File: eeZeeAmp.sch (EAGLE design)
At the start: 15 parts, among them IC1 LM386

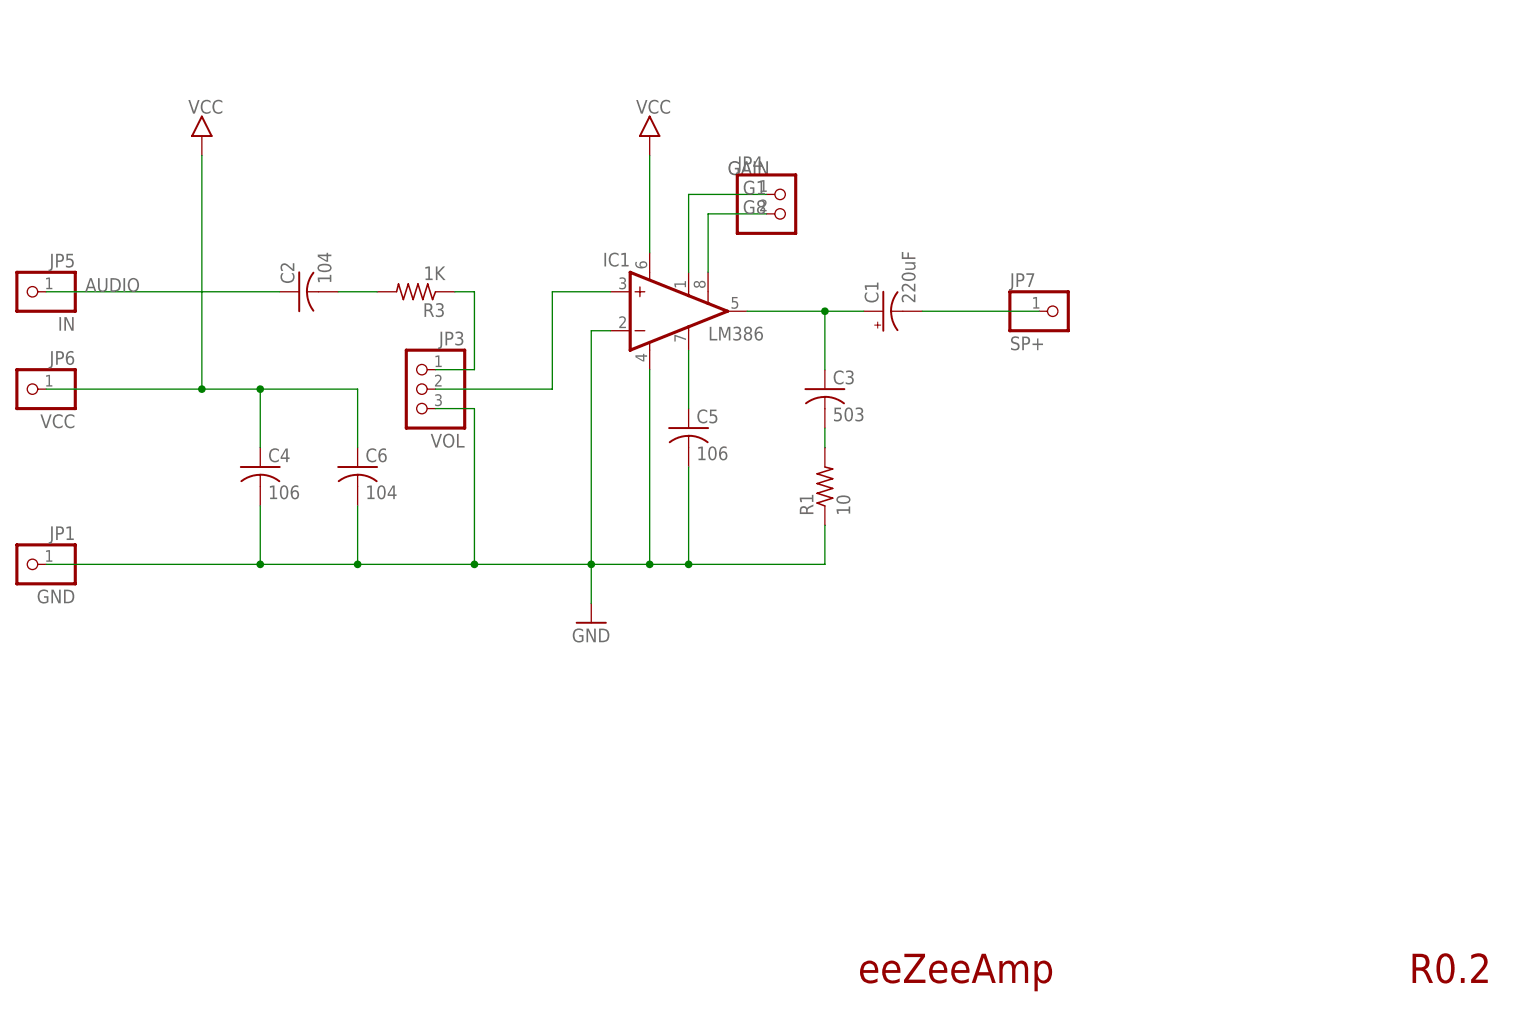
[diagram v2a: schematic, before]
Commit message: Separated gain pin header into individual pins
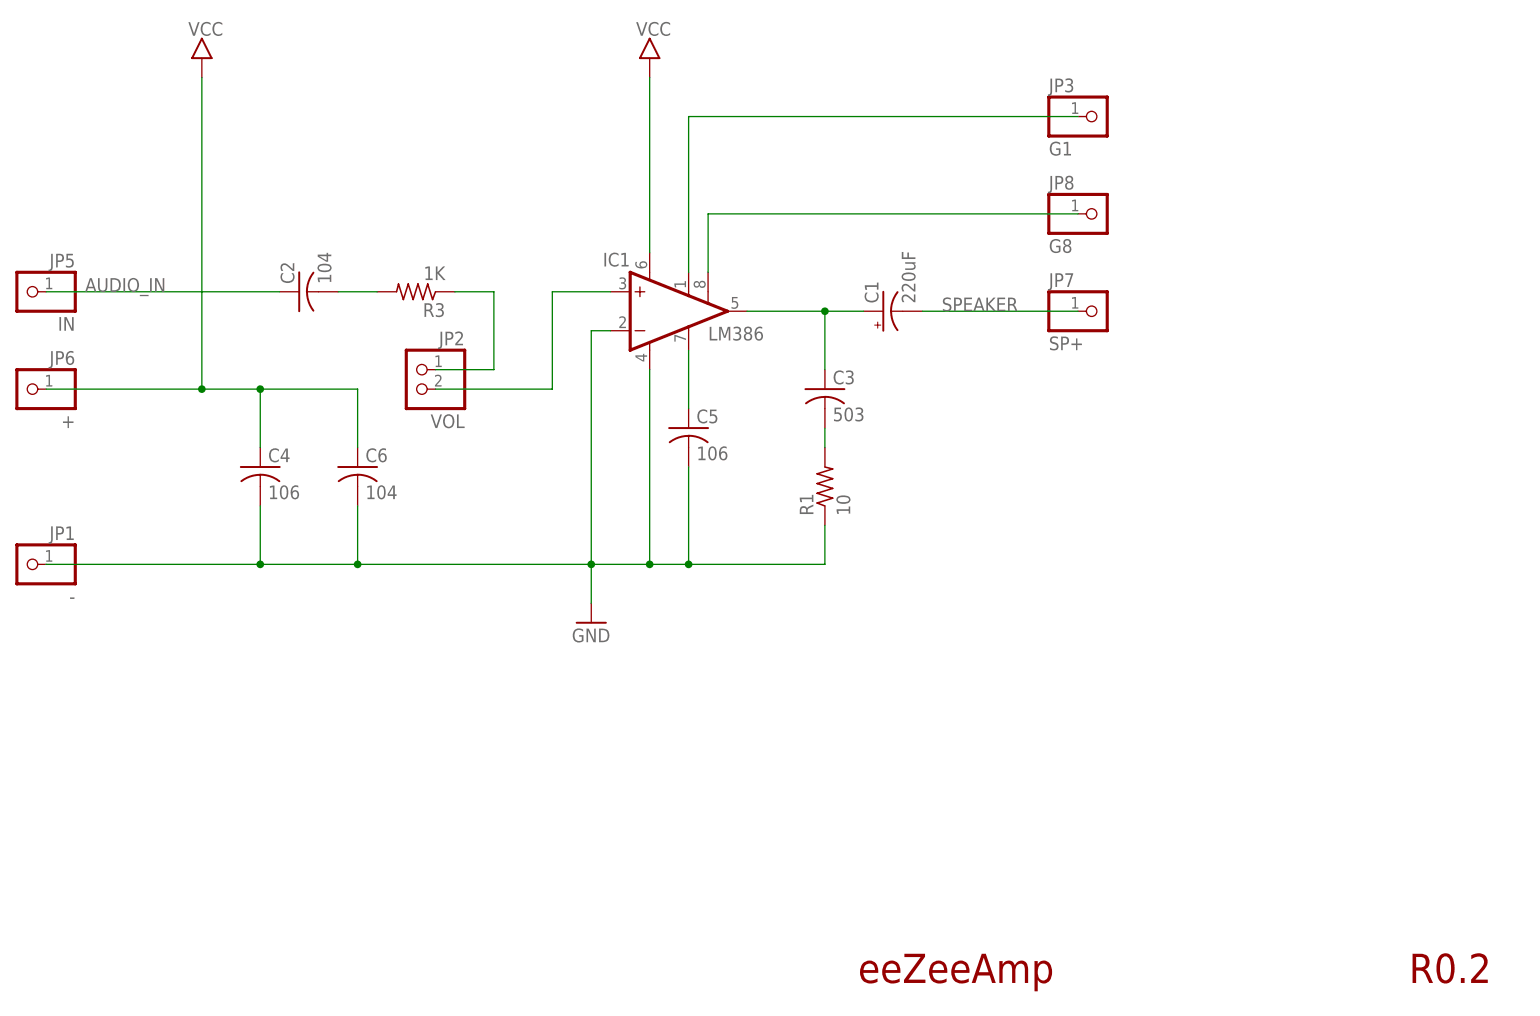
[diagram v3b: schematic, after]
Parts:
- removed JP4: (no value), pinhead-2:PINHD-1X02_2.54-S
- added JP2: VOL, pinhead-2:PINHD-1X02_2.54-S
- added JP8: G8, pinhead-2:PINHD-1X01_2.54-S
- JP1: value GND -> -
- JP3: value VOL -> G1; device pinhead-2:PINHD-1X03_2.54-S -> pinhead-2:PINHD-1X01_2.54-S
- JP6: value VCC -> +
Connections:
- net AUDIO renamed AUDIO_IN
- net SP+ renamed SPEAKER
- net G1: now also JP3.1; no longer JP4.1
- net G8: now also JP8.1; no longer JP4.2
- net GND: no longer JP3.3
- net N$1: now also JP2.2; no longer JP3.2
- net N$8: now also JP2.1; no longer JP3.1
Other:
- note removed: "GAIN"
- moved on the sheet: JP7
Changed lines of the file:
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@@
 <part name="FRAME1" library="bt" deviceset="LETTER_L" device=""/>
 <part name="C6" library="rcl" deviceset="C-US" device="C0603" value="104"/>
-<part name="JP3" library="pinhead-2" deviceset="PINHD-1X03" device="_2.54-S" value="VOL"/>
-<part name="JP4" library="pinhead-2" deviceset="PINHD-1X02" device="_2.54-S"/>
 <part name="JP5" library="pinhead-2" deviceset="PINHD-1X01" device="_2.54-S" value="IN"/>
-<part name="JP6" library="pinhead-2" deviceset="PINHD-1X01" device="_2.54-S" value="VCC"/>
+<part name="JP6" library="pinhead-2" deviceset="PINHD-1X01" device="_2.54-S" value="+"/>
 <part name="JP7" library="pinhead-2" deviceset="PINHD-1X01" device="_2.54-S" value="SP+"/>
-<part name="JP1" library="pinhead-2" deviceset="PINHD-1X01" device="_2.54-S" value="GND"/>
+<part name="JP1" library="pinhead-2" deviceset="PINHD-1X01" device="_2.54-S" value="-"/>
+<part name="JP2" library="pinhead-2" deviceset="PINHD-1X02" device="_2.54-S" value="VOL"/>
+<part name="JP3" library="pinhead-2" deviceset="PINHD-1X01" device="_2.54-S" value="G1"/>
+<part name="JP8" library="pinhead-2" deviceset="PINHD-1X01" device="_2.54-S" value="G8"/>
 </parts>
 <sheets>
@@
 <text x="159.258" y="24.13" size="3.81" layer="94">eeZeeAmp</text>
 <text x="231.14" y="24.13" size="3.81" layer="94">R0.2</text>
-<text x="142.24" y="129.54" size="1.778" layer="97">GAIN</text>
 </plain>
 <instances>
@@
 <instance part="R1" gate="G$1" x="154.94" y="88.9" rot="R90"/>
 <instance part="R3" gate="G$1" x="101.6" y="114.3" rot="R180"/>
-<instance part="U$1" gate="G$1" x="132.08" y="132.08"/>
-<instance part="U$2" gate="G$1" x="73.66" y="132.08"/>
+<instance part="U$1" gate="G$1" x="132.08" y="142.24"/>
+<instance part="U$2" gate="G$1" x="73.66" y="142.24"/>
 <instance part="C4" gate="G$1" x="81.28" y="91.44"/>
 <instance part="GND1" gate="1" x="124.46" y="71.12"/>
@@
 <instance part="FRAME1" gate="G$2" x="147.32" y="2.54"/>
 <instance part="C6" gate="G$1" x="93.98" y="91.44"/>
-<instance part="JP3" gate="A" x="101.6" y="101.6" rot="MR0"/>
-<instance part="JP4" gate="A" x="149.86" y="124.46"/>
 <instance part="JP5" gate="A" x="50.8" y="114.3" rot="MR0"/>
 <instance part="JP6" gate="A" x="50.8" y="101.6" rot="MR0"/>
-<instance part="JP7" gate="A" x="185.42" y="111.76"/>
+<instance part="JP7" gate="A" x="190.5" y="111.76"/>
 <instance part="JP1" gate="A" x="50.8" y="78.74" rot="MR0"/>
+<instance part="JP2" gate="A" x="101.6" y="101.6" rot="MR0"/>
+<instance part="JP3" gate="A" x="190.5" y="137.16"/>
+<instance part="JP8" gate="A" x="190.5" y="124.46"/>
 </instances>
 <busses>
@@
 <wire x1="127" y1="114.3" x2="119.38" y2="114.3" width="0.1524" layer="91"/>
 <wire x1="119.38" y1="114.3" x2="119.38" y2="101.6" width="0.1524" layer="91"/>
-<pinref part="JP3" gate="A" pin="2"/>
 <wire x1="119.38" y1="101.6" x2="104.14" y2="101.6" width="0.1524" layer="91"/>
+<pinref part="JP2" gate="A" pin="2"/>
 </segment>
 </net>
@@
 </segment>
 </net>
-<net name="SP+" class="0">
+<net name="SPEAKER" class="0">
 <segment>
 <pinref part="C1" gate="G$1" pin="-"/>
-<wire x1="167.64" y1="111.76" x2="182.88" y2="111.76" width="0.1524" layer="91"/>
+<wire x1="167.64" y1="111.76" x2="187.96" y2="111.76" width="0.1524" layer="91"/>
 <pinref part="JP7" gate="A" pin="1"/>
+<label x="170.18" y="111.76" size="1.778" layer="95"/>
 </segment>
 </net>
@@
 <segment>
 <pinref part="R3" gate="G$1" pin="1"/>
-<wire x1="106.68" y1="114.3" x2="109.22" y2="114.3" width="0.1524" layer="91"/>
-<pinref part="JP3" gate="A" pin="1"/>
-<wire x1="104.14" y1="104.14" x2="109.22" y2="104.14" width="0.1524" layer="91"/>
-<wire x1="109.22" y1="104.14" x2="109.22" y2="114.3" width="0.1524" layer="91"/>
+<wire x1="106.68" y1="114.3" x2="111.76" y2="114.3" width="0.1524" layer="91"/>
+<wire x1="104.14" y1="104.14" x2="111.76" y2="104.14" width="0.1524" layer="91"/>
+<wire x1="111.76" y1="104.14" x2="111.76" y2="114.3" width="0.1524" layer="91"/>
+<pinref part="JP2" gate="A" pin="1"/>
 </segment>
 </net>
@@
 <segment>
 <pinref part="IC1" gate="G$1" pin="VS"/>
-<wire x1="132.08" y1="119.38" x2="132.08" y2="132.08" width="0.1524" layer="91"/>
+<wire x1="132.08" y1="119.38" x2="132.08" y2="142.24" width="0.1524" layer="91"/>
 <pinref part="U$1" gate="G$1" pin="VCC"/>
 </segment>
 <segment>
-<wire x1="73.66" y1="101.6" x2="73.66" y2="132.08" width="0.1524" layer="91"/>
+<wire x1="73.66" y1="101.6" x2="73.66" y2="142.24" width="0.1524" layer="91"/>
 <pinref part="U$2" gate="G$1" pin="VCC"/>
 <wire x1="53.34" y1="101.6" x2="73.66" y2="101.6" width="0.1524" layer="91"/>
@@
 </segment>
 </net>
-<net name="AUDIO" class="0">
+<net name="AUDIO_IN" class="0">
 <segment>
 <pinref part="C2" gate="G$1" pin="1"/>
@@
 <net name="GND" class="0">
 <segment>
-<wire x1="109.22" y1="99.06" x2="109.22" y2="78.74" width="0.1524" layer="91"/>
 <pinref part="R1" gate="G$1" pin="1"/>
-<wire x1="109.22" y1="78.74" x2="124.46" y2="78.74" width="0.1524" layer="91"/>
 <wire x1="124.46" y1="78.74" x2="132.08" y2="78.74" width="0.1524" layer="91"/>
 <wire x1="132.08" y1="78.74" x2="137.16" y2="78.74" width="0.1524" layer="91"/>
@@
 <junction x="124.46" y="78.74"/>
 <wire x1="53.34" y1="78.74" x2="81.28" y2="78.74" width="0.1524" layer="91"/>
-<junction x="109.22" y="78.74"/>
 <pinref part="C4" gate="G$1" pin="2"/>
 <wire x1="81.28" y1="78.74" x2="93.98" y2="78.74" width="0.1524" layer="91"/>
-<wire x1="93.98" y1="78.74" x2="109.22" y2="78.74" width="0.1524" layer="91"/>
+<wire x1="93.98" y1="78.74" x2="124.46" y2="78.74" width="0.1524" layer="91"/>
 <wire x1="81.28" y1="86.36" x2="81.28" y2="78.74" width="0.1524" layer="91"/>
 <junction x="81.28" y="78.74"/>
@@
 <wire x1="93.98" y1="86.36" x2="93.98" y2="78.74" width="0.1524" layer="91"/>
 <junction x="93.98" y="78.74"/>
-<pinref part="JP3" gate="A" pin="3"/>
-<wire x1="104.14" y1="99.06" x2="109.22" y2="99.06" width="0.1524" layer="91"/>
 <pinref part="JP1" gate="A" pin="1"/>
 </segment>
@@
 <segment>
 <pinref part="IC1" gate="G$1" pin="GAIN@1"/>
-<wire x1="137.16" y1="116.84" x2="137.16" y2="127" width="0.1524" layer="91"/>
-<wire x1="137.16" y1="127" x2="147.32" y2="127" width="0.1524" layer="91"/>
-<label x="147.32" y="127" size="1.778" layer="95" rot="MR0"/>
-<pinref part="JP4" gate="A" pin="1"/>
+<wire x1="137.16" y1="116.84" x2="137.16" y2="137.16" width="0.1524" layer="91"/>
+<wire x1="137.16" y1="137.16" x2="187.96" y2="137.16" width="0.1524" layer="91"/>
+<pinref part="JP3" gate="A" pin="1"/>
 </segment>
 </net>
@@
 <pinref part="IC1" gate="G$1" pin="GAIN@2"/>
 <wire x1="139.7" y1="116.84" x2="139.7" y2="124.46" width="0.1524" layer="91"/>
-<wire x1="139.7" y1="124.46" x2="147.32" y2="124.46" width="0.1524" layer="91"/>
-<label x="147.32" y="124.46" size="1.778" layer="95" rot="MR0"/>
-<pinref part="JP4" gate="A" pin="2"/>
+<wire x1="139.7" y1="124.46" x2="187.96" y2="124.46" width="0.1524" layer="91"/>
+<pinref part="JP8" gate="A" pin="1"/>
 </segment>
 </net>
